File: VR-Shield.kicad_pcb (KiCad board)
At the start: 2 copper layers, 6.4 x 6.4 mm, 22 parts, among them Q1 IRF7404, Q2 BC847, U1 ESP32 WROOM32 Devkit, U2 MCP73831-2-OT

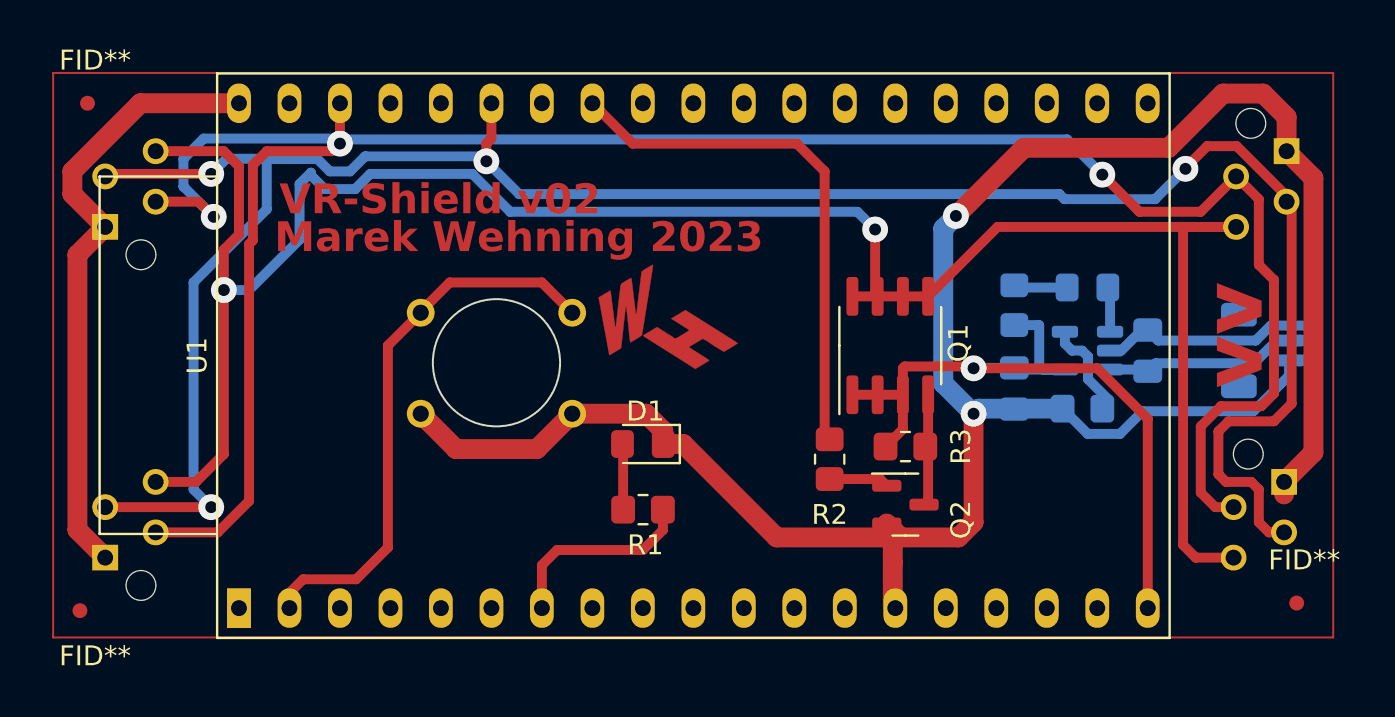
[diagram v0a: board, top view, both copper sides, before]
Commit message: Fixed issues with pad size and distance Please enter the commit message for your changes. Lines starting
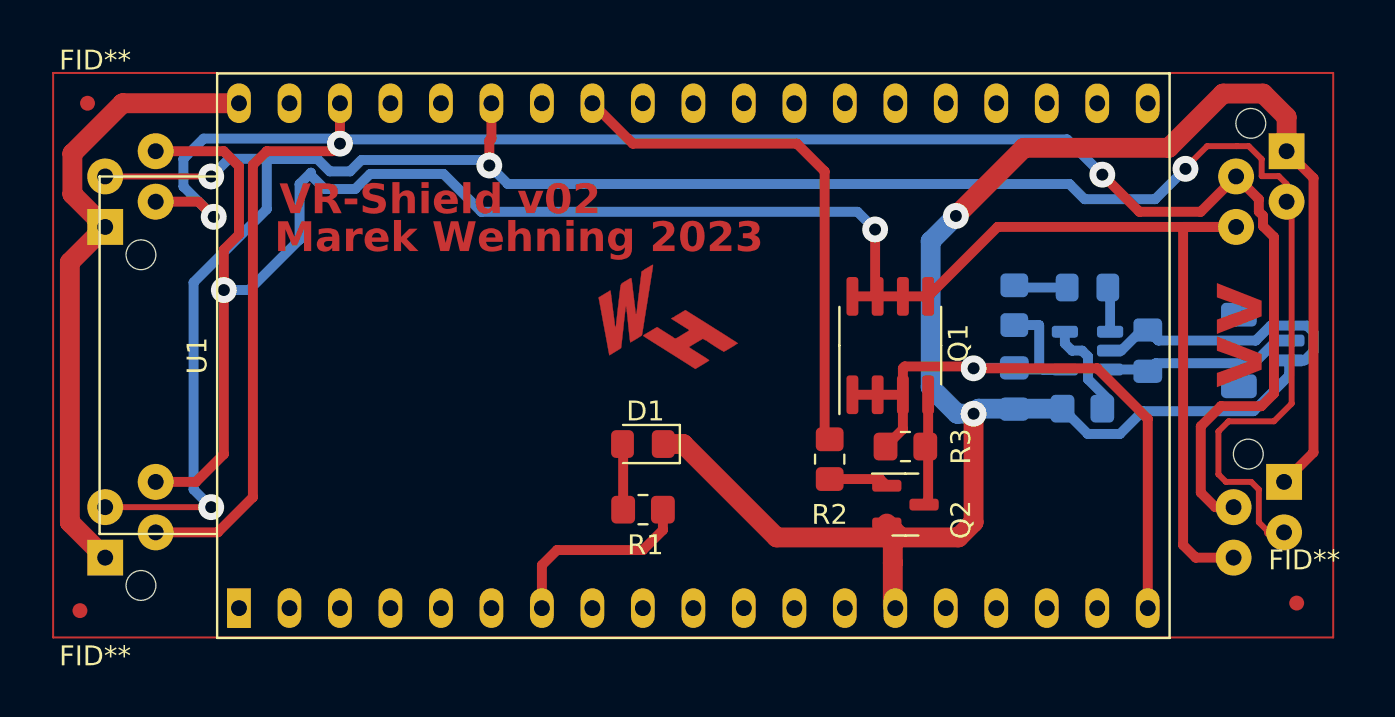
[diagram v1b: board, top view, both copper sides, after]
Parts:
- removed CB1: RST, Button_Switch_THT:SW_Tactile_Straight_KSA0Axx1LFTR
- P1, P2, P3, P4: footprint Connector_TE-Connectivity:TE_Micro-MaTch_215079-4_2x02_P1.27mm_Vertical -> Custom:TE_Micro-MaTch_215079-4_2x02_P1.27mm_Vertical
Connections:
- U1 pad 14: GND -> unconnected-(U1-GND-Pad14)
- U1 pad 2: Net-(U1-CHIP_PU) -> unconnected-(U1-CHIP_PU-Pad2)
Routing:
- net Net-(U1-CHIP_PU): track 28.1 -> 0.00 mm
- net GND: track 156.8 -> 143.3 mm
- net Net-(P1-SDA): track 116.2 -> 117.1 mm
- net unconnected-(U1-CHIP_PU-Pad2): track 0.00 -> 0.76 mm
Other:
- board outline removed

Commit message: t V03!!!!
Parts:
- removed BT1: Battery_Cell, Connector_JST:JST_SH_BM02B-SRSS-TB_1x02-1MP_P1.00mm_Vertical
- removed C1: C, Capacitor_SMD:C_0805_2012Metric_Pad1.18x1.45mm_HandSolder
- removed C2: 4,7u, Capacitor_SMD:C_0805_2012Metric_Pad1.18x1.45mm_HandSolder
- removed D2: GREEN, LED_SMD:LED_0805_2012Metric_Pad1.15x1.40mm_HandSolder
- removed P1, P2, P3, P4: ~, Custom:TE_Micro-MaTch_215079-4_2x02_P1.27mm_Vertical
- removed R4: 10k, Resistor_SMD:R_0805_2012Metric_Pad1.20x1.40mm_HandSolder
- removed R5: 470, Resistor_SMD:R_0805_2012Metric_Pad1.20x1.40mm_HandSolder
- removed U2: MCP73831-2-OT, Package_TO_SOT_SMD:SOT-23-5
- added ?: , , F.Cu at (60.7, 19.6)
- added J1: Double I2C Socket, Custom:Custom Socket I2C, F.Cu at (18.6, 28.2)
- added J5: Double I2C Socket, Custom:Custom Socket I2C, F.Cu at (73.8, 28.2)
- added REF**: MountingHole_2.2mm_M2_ISO7380_Pad, MountingHole:MountingHole_2.2mm_M2_ISO7380_Pad, F.Cu at (31.5, 37.1)
- moved FID** 24.6 mm to (72.6, 16.5)
- moved Q1 11.3 mm to (45.3, 24.2)
- moved R3 11.1 mm to (46.1, 29.7)
- moved Q2 11.1 mm to (46.1, 32.6)
- moved R2 10.5 mm to (42.9, 30.5)
- moved R1 5.02 mm to (38.6, 36.8), turned to 90 degrees
- moved D1 4.07 mm to (39.6, 33.8)
- moved FID** 3.75 mm to (18.5, 39.4)
- moved FID** 3.36 mm to (18.5, 17.3)
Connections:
- net Net-(P1-VCC) renamed /VCC
- U1 pad 33: Net-(P1-SDA) -> /SDA
- U1 pad 36: Net-(P1-SCL) -> /SCL
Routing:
- net /SDA: track 0.00 -> 124.1 mm, vias 0 -> 3
- net Net-(P1-SDA): track 117.1 -> 0.00 mm, vias 4 -> 0
- net Net-(P1-SCL): track 113.3 -> 0.00 mm, vias 3 -> 0
- net GND: track 143.3 -> 39.2 mm, vias 2 -> 5
- net /SCL: track 0.00 -> 98.2 mm, vias 0 -> 4
- net /VCC: track 107.7 -> 86.1 mm, vias 2 -> 0
- net Net-(BT1-+): track 9.68 -> 0.00 mm
- net Net-(U1-GPIO19): track 26.7 -> 18.7 mm, vias 0 -> 2
- net /LED: track 10.0 -> 3.23 mm
- net Net-(U2-PROG): track 5.16 -> 0.00 mm
- net Net-(Q1-G): track 5.73 -> 2.95 mm
- net Net-(D2-A): track 2.70 -> 0.00 mm
- net Net-(D2-K): track 2.27 -> 0.00 mm
- net /5V: track 39.1 -> 41.1 mm, vias 1 -> 0
- net Net-(D1-A): track 3.32 -> 2.07 mm
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- added copper zone on B.Cu, net GND
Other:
- board outline added: 64.4 x 28.4 mm
- board text added: "+"
- board text added: "MWeh 2023"
- board text added: "VR-Shield v03.1"
- board text removed: "Marek Wehning 2023"
- board text removed: "VR-Shield v02"
- board text removed: "vv"

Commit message: User friendlyness improved
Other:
- board text added: "USB"
- board text added: "VR-Shield v03.2"
- board text removed: "VR-Shield v03.1"
